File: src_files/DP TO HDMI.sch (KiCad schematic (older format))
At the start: 38 parts

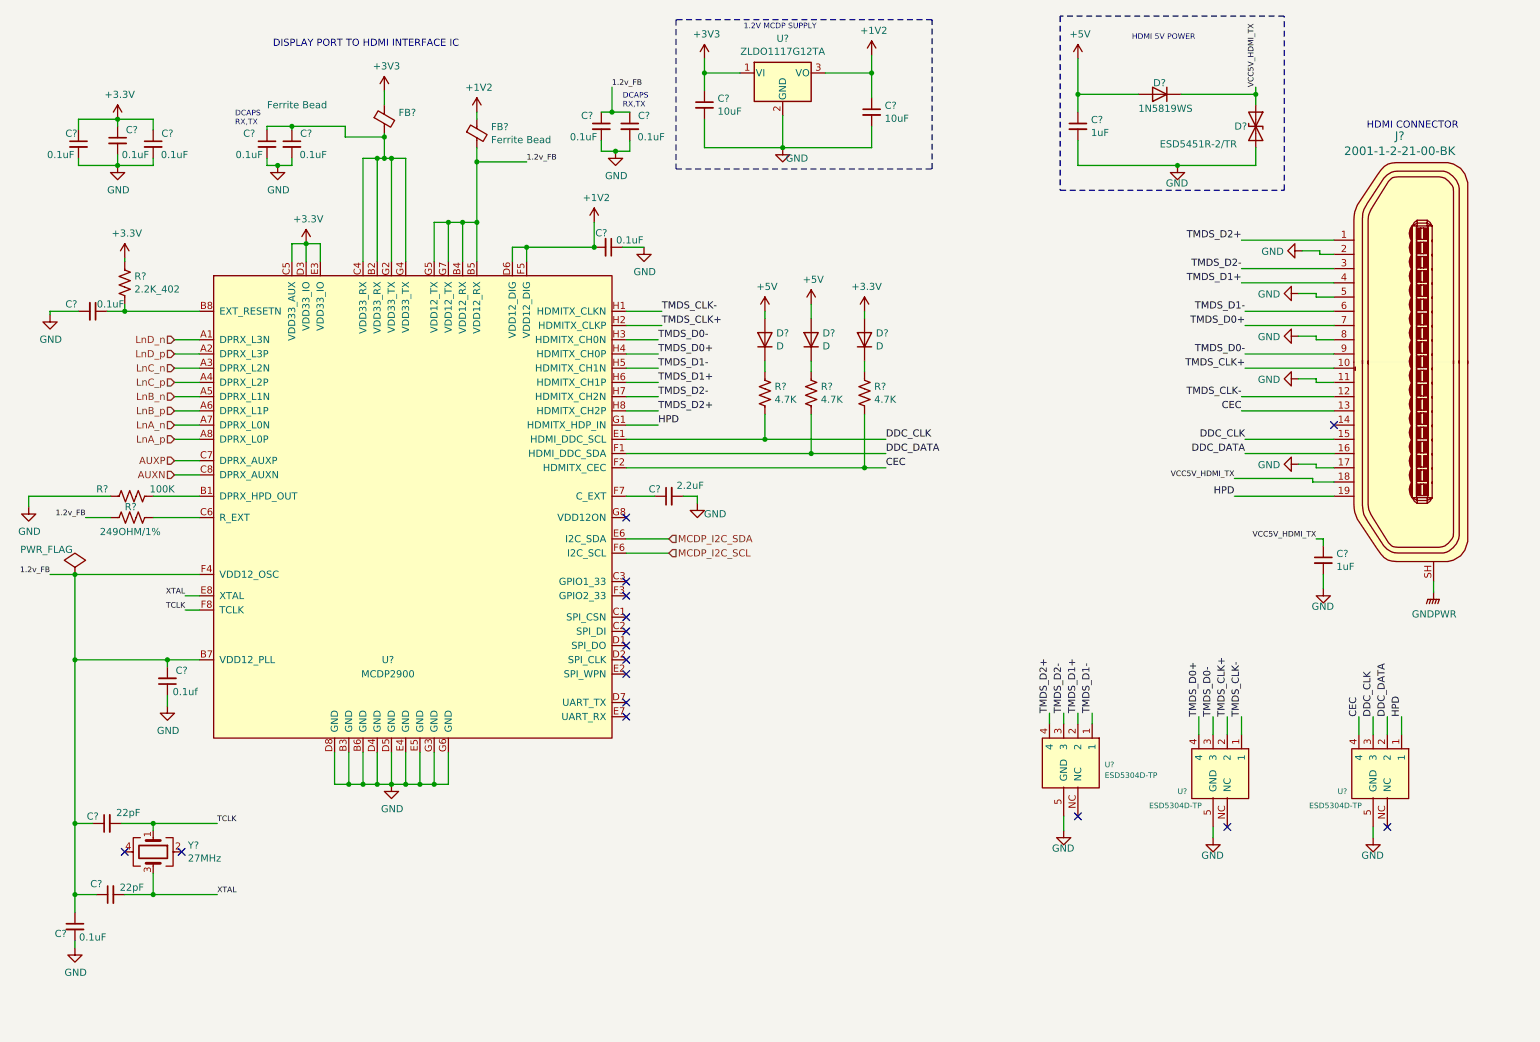
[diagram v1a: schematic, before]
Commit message: schematic capture complete
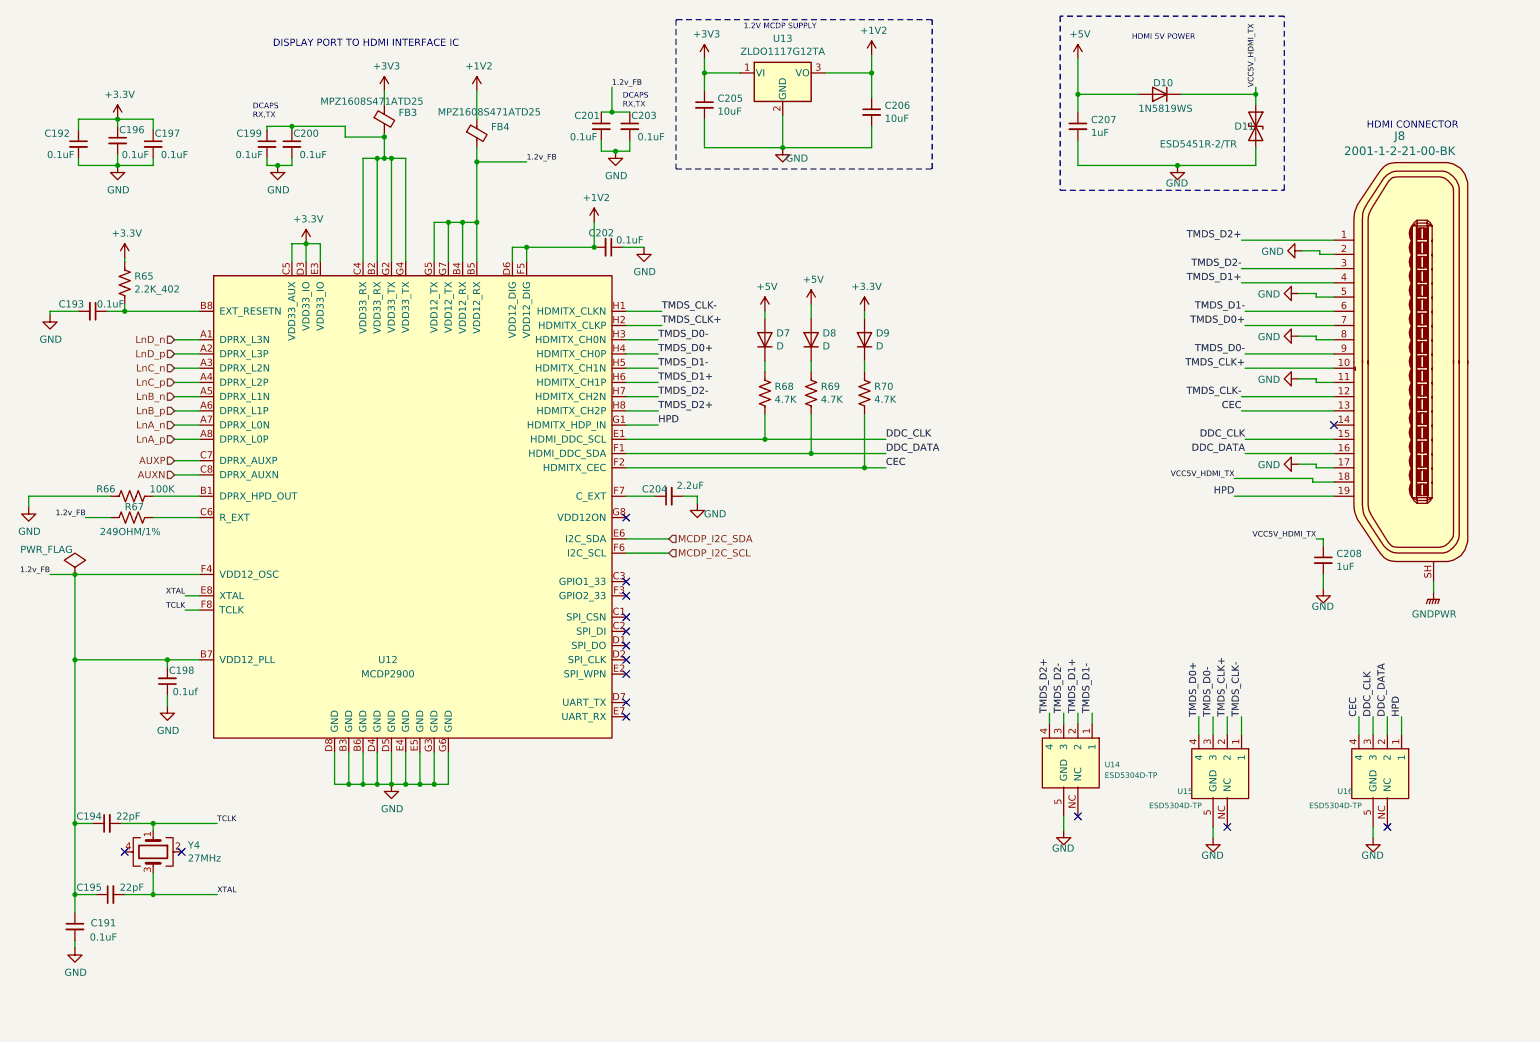
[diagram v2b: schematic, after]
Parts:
- C207, C208: renamed from C?; footprint (none) -> Capacitor_SMD:C_0402_1005Metric
- D7, D8, D9: renamed from D?; footprint Diode_SMD:D_SOD-323 -> Diode_SMD:D_SOD-123
- FB3, FB4: renamed from FB?; value Ferrite Bead -> MPZ1608S471ATD25
- Y4: renamed from Y?; footprint Crystal:Crystal_HC33-U_Horizontal_1EP_style1 -> Crystal:Crystal_SMD_2016-4Pin_2.0x1.6mm; Mfr No. ABM8G-27.000MHZ-B4Y-T -> 402F27011CAR
- gave numbers to parts that had none: 30

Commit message: updated footprint and schematics
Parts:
- removed J8: 2001-1-2-21-00-BK, digikey-footprints:HDMI_Mini_Female_2001-1-2-21-00-BK, symbol dk_USB-DVI-HDMI-Connectors:2001-1-2-21-00-BK
- added J?: 3-1734592-0, greencharge-footprints:TE_3-1734592-0, symbol 3-1734592-0:3-1734592-0
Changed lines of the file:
@@
 $Descr A4 11693 8268
 encoding utf-8
-Sheet 7 15
+Sheet 7 16
 Title ""
 Date ""
@@
 NoConn ~ 9100 6200
 $Comp
-L dk_USB-DVI-HDMI-Connectors:2001-1-2-21-00-BK J?
-U 1 1 637EF133
-P 10450 2975
-AR Path="/61C73AB6/637EF133" Ref="J?"  Part="1"
-AR Path="/61C73AB6/635B9242/637EF133" Ref="J8"  Part="1"
-F 0 "J8" H 10588 4607 60  0000 C CNN
-F 1 "2001-1-2-21-00-BK" H 10588 4501 60  0000 C CNN
-F 2 "digikey-footprints:HDMI_Mini_Female_2001-1-2-21-00-BK" H 10650 3175 60  0001 L CNN
-F 3 "http://cnctech.us/pdfs/2001-1-2-21-00-BK.pdf" H 10650 3275 60  0001 L CNN
-F 4 "1175-1704-1-ND" H 10650 3375 60  0001 L CNN "Digi-Key_PN"
-F 5 "2001-1-2-21-00-BK" H 10650 3475 60  0001 L CNN "MPN"
-F 6 "Connectors, Interconnects" H 10650 3575 60  0001 L CNN "Category"
-F 7 "USB, DVI, HDMI Connectors" H 10650 3675 60  0001 L CNN "Family"
-F 8 "http://cnctech.us/pdfs/2001-1-2-21-00-BK.pdf" H 10650 3775 60  0001 L CNN "DK_Datasheet_Link"
-F 9 "/product-detail/en/cnc-tech/2001-1-2-21-00-BK/1175-1704-1-ND/4867013" H 10650 3875 60  0001 L CNN "DK_Detail_Page"
-F 10 "CONN RCPT MINI HDMI 19POS SMD RA" H 10650 3975 60  0001 L CNN "Description"
-F 11 "CNC Tech" H 10650 4075 60  0001 L CNN "Manufacturer"
-F 12 "Active" H 10650 4175 60  0001 L CNN "Status"
-	1    10450 2975
-	-1   0    0    -1
-$EndComp
-$Comp
 L OLIMEX_Power:GND #PWR?
 U 1 1 637EF13C
@@
 Wire Wire Line
 	9850 2075 9200 2075
-$Comp
-L power:GNDPWR #PWR?
-U 1 1 637EF181
-P 10550 4550
-AR Path="/61C73AB6/637EF181" Ref="#PWR?"  Part="1"
-AR Path="/61C73AB6/635B9242/637EF181" Ref="#PWR0207"  Part="1"
-F 0 "#PWR0207" H 10550 4350 50  0001 C CNN
-F 1 "GNDPWR" H 10554 4396 50  0000 C CNN
-F 2 "" H 10550 4500 50  0001 C CNN
-F 3 "" H 10550 4500 50  0001 C CNN
-	1    10550 4550
-	1    0    0    -1
-$EndComp
-Wire Wire Line
-	10550 4550 10550 4475
 $Comp
 L Device:C_Small C?
@@
 	0    -1   -1   0
 $EndComp
+Wire Wire Line
+	10750 5200 10750 5125
+$Comp
+L power:GNDPWR #PWR?
+U 1 1 637EF181
+P 10750 5200
+AR Path="/61C73AB6/637EF181" Ref="#PWR?"  Part="1"
+AR Path="/61C73AB6/635B9242/637EF181" Ref="#PWR0207"  Part="1"
+F 0 "#PWR0207" H 10750 5000 50  0001 C CNN
+F 1 "GNDPWR" H 10754 5046 50  0000 C CNN
+F 2 "" H 10750 5150 50  0001 C CNN
+F 3 "" H 10750 5150 50  0001 C CNN
+	1    10750 5200
+	1    0    0    -1
+$EndComp
+$Sheet
+S 4000 6000 2625 1525
+U 6311BE81
+F0 "Sheet6311BE80" 50
+F1 "hdmi to mipi.sch" 50
+$EndSheet
+$Comp
+L 3-1734592-0:3-1734592-0 J?
+U 1 1 631A8114
+P 10700 3300
+AR Path="/631A8114" Ref="J?"  Part="1"
+AR Path="/61C73AB6/631A8114" Ref="J?"  Part="1"
+AR Path="/62F6D336/631A8114" Ref="J?"  Part="1"
+AR Path="/61C73AB6/635B9242/631A8114" Ref="J?"  Part="1"
+F 0 "J?" V 11075 3250 50  0000 C CNN
+F 1 "3-1734592-0" V 11166 3250 50  0000 C CNN
+F 2 "greencharge-footprints:TE_3-1734592-0" H 10700 3300 50  0001 L BNN
+F 3 "" H 10700 3300 50  0001 L BNN
+F 4 "TE Connectivity" H 10700 3300 50  0001 L BNN "MANUFACTURER"
+F 5 "2.05mm" H 10700 3300 50  0001 L BNN "MAXIMUM_PACKAGE_HEIGHT"
+F 6 "Manufacturer Recommendations" H 10700 3300 50  0001 L BNN "STANDARD"
+F 7 "C" H 10700 3300 50  0001 L BNN "PARTREV"
+	1    10700 3300
+	1    0    0    -1
+$EndComp
 $EndSCHEMATC

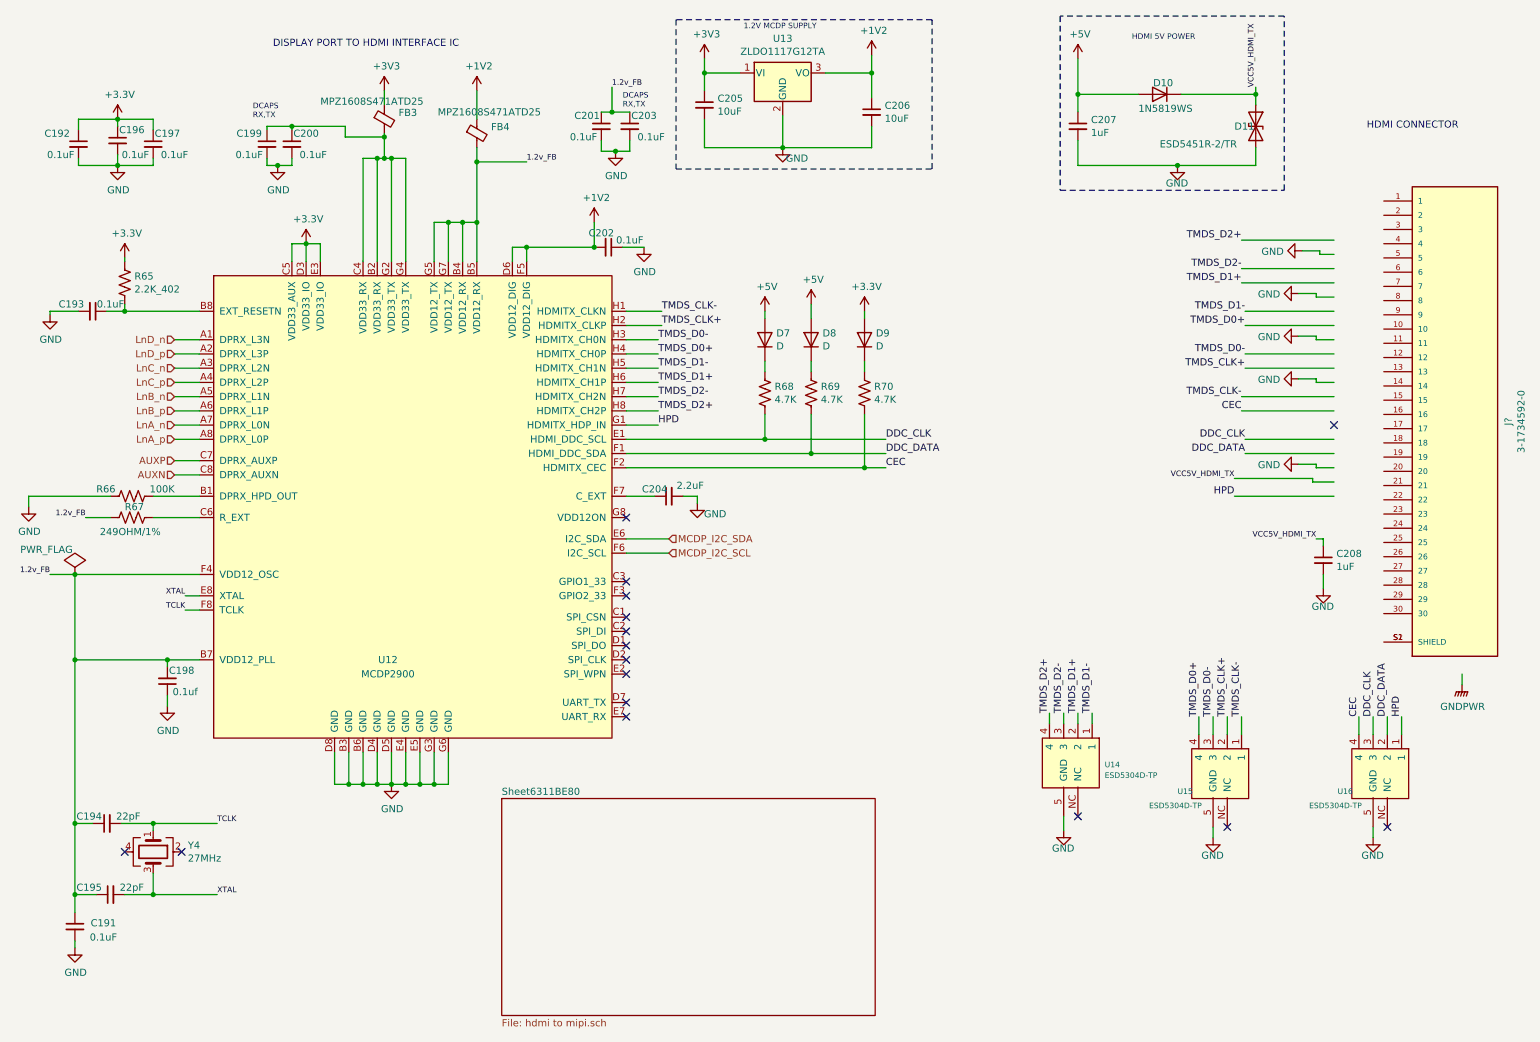
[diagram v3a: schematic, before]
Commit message: update 1 extra hdmi to mipi interface
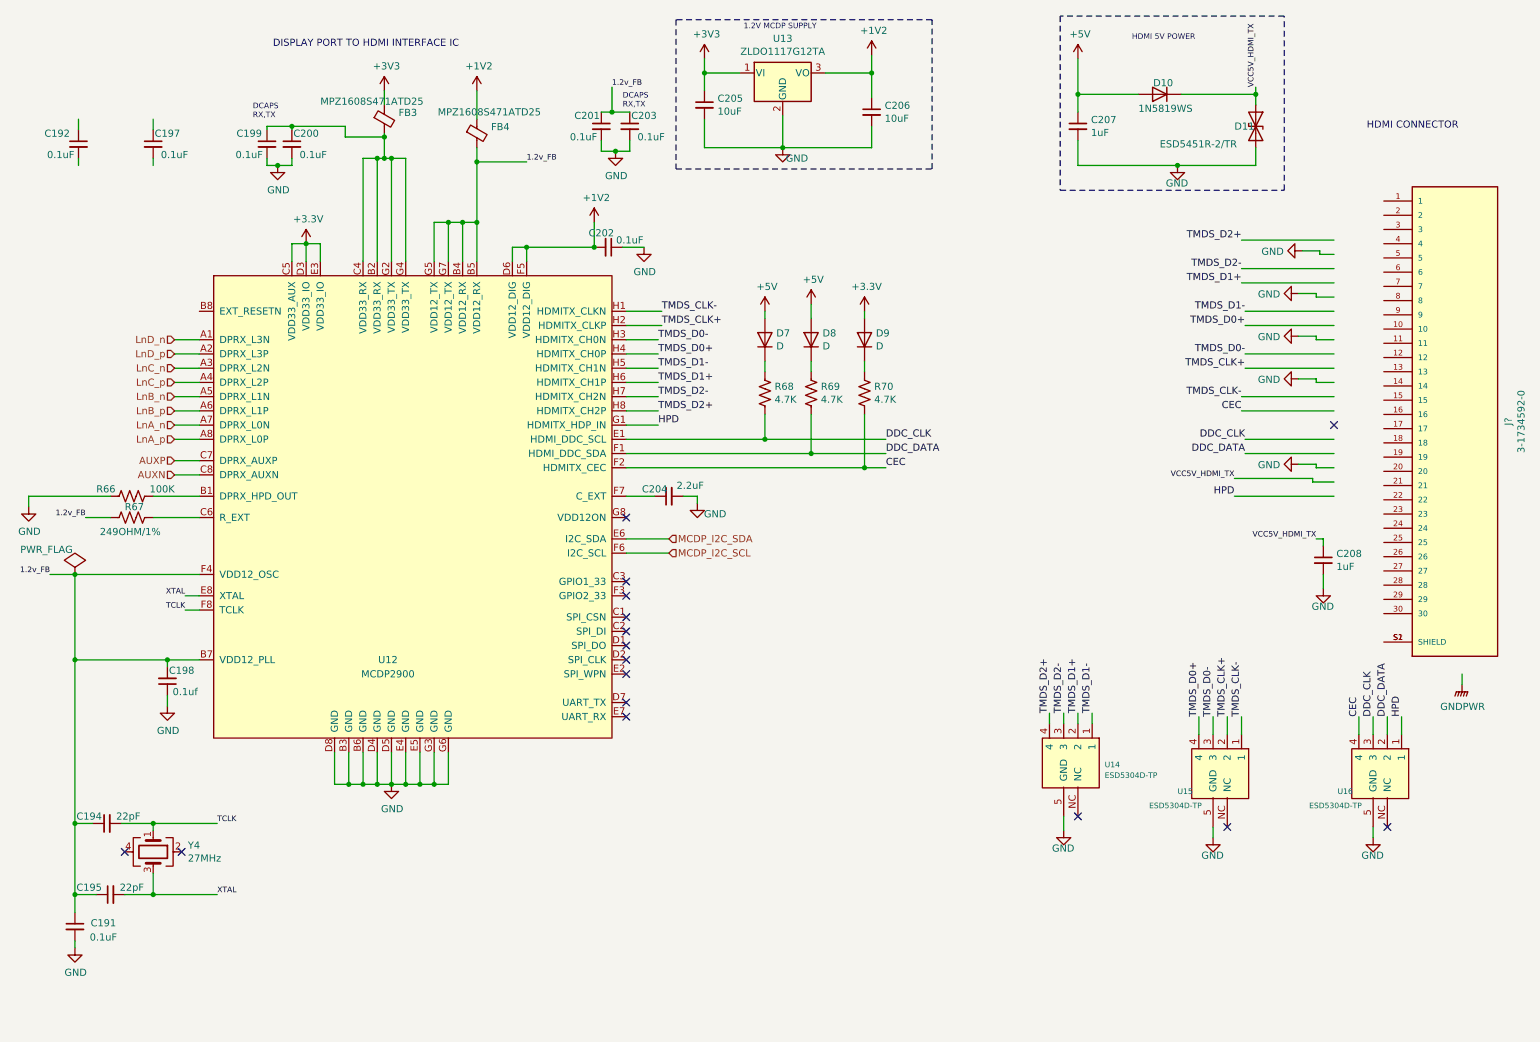
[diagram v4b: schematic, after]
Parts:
- removed C193, C196: 0.1uF, Capacitor_SMD:C_0402_1005Metric, symbol Device:C_Small
- removed R65: 2.2K_402, Resistor_SMD:R_0402_1005Metric, symbol Device:R_US
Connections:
- wire segments 218 -> 206
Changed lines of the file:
@@
 $Descr A4 11693 8268
 encoding utf-8
-Sheet 7 16
+Sheet 7 15
 Title ""
 Date ""
@@
 	3125 5675 3125 5900
 Connection ~ 3125 5900
-$Comp
-L OLIMEX_Power:+3.3V #PWR?
-U 1 1 635D8DE7
-P 1350 2200
-AR Path="/61B4DD57/635D8DE7" Ref="#PWR?"  Part="1"
-AR Path="/61C73AB6/635B9242/635D8DE7" Ref="#PWR077"  Part="1"
-F 0 "#PWR077" H 1350 2050 50  0001 C CNN
-F 1 "+3.3V" H 1365 2373 50  0000 C CNN
-F 2 "" H 1350 2200 60  0000 C CNN
-F 3 "" H 1350 2200 60  0000 C CNN
-	1    1350 2200
-	1    0    0    -1
-$EndComp
-$Comp
-L Device:R_US R?
-U 1 1 635D8DEE
-P 1350 2375
-AR Path="/61B4DD57/635D8DEE" Ref="R?"  Part="1"
-AR Path="/61C73AB6/635B9242/635D8DEE" Ref="R65"  Part="1"
-F 0 "R65" H 1418 2421 50  0000 L CNN
-F 1 "2.2K_402" H 1418 2330 50  0000 L CNN
-F 2 "Resistor_SMD:R_0402_1005Metric" V 1390 2365 50  0001 C CNN
-F 3 "~" H 1350 2375 50  0001 C CNN
-F 4 "0402WGJ0222TCE" H 1350 2375 50  0001 C CNN "Mfr No."
-	1    1350 2375
-	1    0    0    -1
-$EndComp
-Wire Wire Line
-	1350 2225 1350 2200
-Wire Wire Line
-	1350 2525 1350 2575
-Wire Wire Line
-	1875 2575 1350 2575
 $Comp
 L Device:R_US R?
@@
 	1    0    0    -1
 $EndComp
-$Comp
-L Device:C_Small C?
-U 1 1 635D8F3D
-P 1300 1375
-AR Path="/61B4DD57/635D8F3D" Ref="C?"  Part="1"
-AR Path="/61C73AB6/635B9242/635D8F3D" Ref="C196"  Part="1"
-F 0 "C196" H 1400 1450 50  0000 C CNN
-F 1 "0.1uF" H 1425 1275 50  0000 C CNN
-F 2 "Capacitor_SMD:C_0402_1005Metric" H 1300 1375 50  0001 C CNN
-F 3 "~" H 1300 1375 50  0001 C CNN
-	1    1300 1375
-	1    0    0    -1
-$EndComp
-Wire Wire Line
-	1300 1475 1300 1550
 Wire Wire Line
 	1550 1550 1550 1500
@@
 	1    0    0    -1
 $EndComp
-$Comp
-L OLIMEX_Power:+3.3V #PWR?
-U 1 1 635D8F4B
-P 1300 1225
-AR Path="/61B4DD57/635D8F4B" Ref="#PWR?"  Part="1"
-AR Path="/61C73AB6/635B9242/635D8F4B" Ref="#PWR075"  Part="1"
-F 0 "#PWR075" H 1300 1075 50  0001 C CNN
-F 1 "+3.3V" H 1315 1398 50  0000 C CNN
-F 2 "" H 1300 1225 60  0000 C CNN
-F 3 "" H 1300 1225 60  0000 C CNN
-	1    1300 1225
-	1    0    0    -1
-$EndComp
 Wire Wire Line
 	1025 1300 1025 1225
 Wire Wire Line
-	1025 1225 1300 1225
-Wire Wire Line
-	1300 1275 1300 1225
-Connection ~ 1300 1225
-Wire Wire Line
 	1550 1300 1550 1225
 Wire Wire Line
-	1550 1225 1300 1225
-Wire Wire Line
 	1025 1500 1025 1550
-Wire Wire Line
-	1025 1550 1300 1550
-Connection ~ 1300 1550
-Wire Wire Line
-	1300 1550 1550 1550
-$Comp
-L OLIMEX_Power:GND #PWR?
-U 1 1 635D8F5B
-P 1300 1550
-AR Path="/61B4DD57/635D8F5B" Ref="#PWR?"  Part="1"
-AR Path="/61C73AB6/635B9242/635D8F5B" Ref="#PWR076"  Part="1"
-F 0 "#PWR076" H 1300 1300 50  0001 C CNN
-F 1 "GND" H 1305 1377 50  0000 C CNN
-F 2 "" H 1300 1550 60  0000 C CNN
-F 3 "" H 1300 1550 60  0000 C CNN
-	1    1300 1550
-	1    0    0    -1
-$EndComp
 NoConn ~ 4875 5325
 NoConn ~ 4875 5425
@@
 	1    0    0    -1
 $EndComp
-$Comp
-L Device:C_Small C?
-U 1 1 635D8FE5
-P 1125 2575
-AR Path="/61B4DD57/635D8FE5" Ref="C?"  Part="1"
-AR Path="/61C73AB6/635B9242/635D8FE5" Ref="C193"  Part="1"
-F 0 "C193" V 1075 2425 50  0000 C CNN
-F 1 "0.1uF" V 1075 2700 50  0000 C CNN
-F 2 "Capacitor_SMD:C_0402_1005Metric" H 1125 2575 50  0001 C CNN
-F 3 "~" H 1125 2575 50  0001 C CNN
-	1    1125 2575
-	0    1    1    0
-$EndComp
-$Comp
-L OLIMEX_Power:GND #PWR?
-U 1 1 635D8FEB
-P 825 2600
-AR Path="/61B4DD57/635D8FEB" Ref="#PWR?"  Part="1"
-AR Path="/61C73AB6/635B9242/635D8FEB" Ref="#PWR073"  Part="1"
-F 0 "#PWR073" H 825 2350 50  0001 C CNN
-F 1 "GND" H 830 2427 50  0000 C CNN
-F 2 "" H 825 2600 60  0000 C CNN
-F 3 "" H 825 2600 60  0000 C CNN
-	1    825  2600
-	1    0    0    -1
-$EndComp
-Wire Wire Line
-	1350 2575 1225 2575
-Wire Wire Line
-	825  2575 825  2600
-Wire Wire Line
-	1025 2575 825  2575
-Connection ~ 1350 2575
 Wire Wire Line
 	6175 2525 6175 2625
@@
 	1    0    0    -1
 $EndComp
-$Sheet
-S 4000 6000 2625 1525
-U 6311BE81
-F0 "Sheet6311BE80" 50
-F1 "hdmi to mipi.sch" 50
-$EndSheet
 $Comp
 L 3-1734592-0:3-1734592-0 J?
